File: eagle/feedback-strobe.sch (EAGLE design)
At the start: 21 parts, among them J2 MOTOR, U1 STN3NF06L, U2 +12v

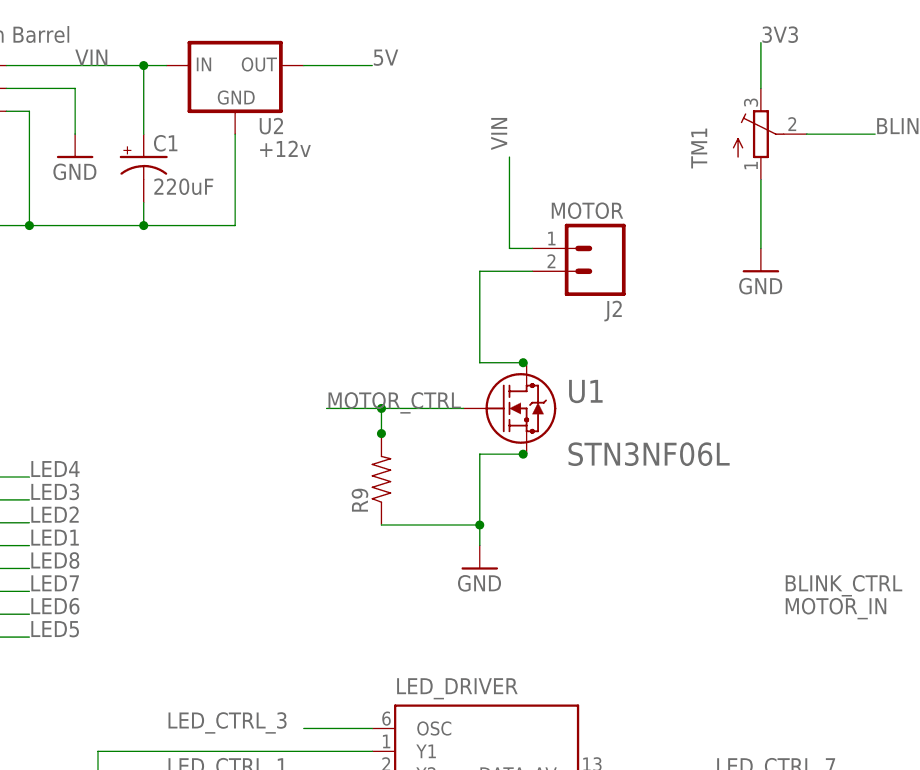
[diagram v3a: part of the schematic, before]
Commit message: added new voltage regulator, reduced number of vias, added more spacing between traces.
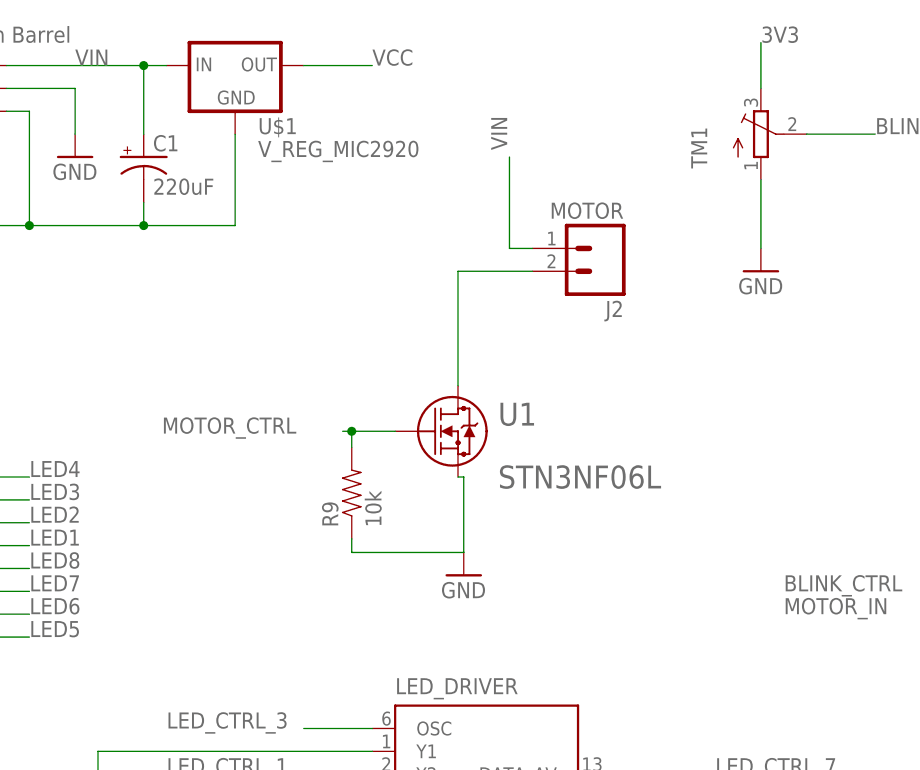
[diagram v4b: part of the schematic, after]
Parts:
- removed U2: +12v, SparkFun-PowerIC:V_REG_78XX7812
- added U$1: V_REG_MIC2920, SparkFun-PowerIC:V_REG_MIC2920
- R9: value (none) -> 10k
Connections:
- removed net N$8: J2.2
- new net N$7: J2.2, U1.2
- new net VCC: U$1.OUT
- net 5V: no longer U2.OUT
- net GND: now also U$1.GND, U1.3; no longer U2.GND
- net VIN: now also U$1.IN; no longer U2.IN
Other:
- moved on the sheet: R9, U1
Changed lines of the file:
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@@
 <setting verticaltext="up"/>
 </settings>
-<grid distance="0.01" unitdist="inch" unit="inch" style="lines" multiple="1" display="no" altdistance="0.01" altunitdist="inch" altunit="inch"/>
+<grid distance="0.1" unitdist="inch" unit="inch" style="lines" multiple="1" display="no" altdistance="0.01" altunitdist="inch" altunit="inch"/>
 <layers>
 <layer number="1" name="Top" color="4" fill="1" visible="no" active="no"/>
@@
 <part name="J2" library="SparkFun-Connectors" deviceset="M02" device="PTH" value="MOTOR"/>
 <part name="DC_IN" library="SparkFun-Connectors" deviceset="POWER_JACK" device="SMD" value="5.5x2.1mm Barrel"/>
-<part name="U2" library="SparkFun-PowerIC" deviceset="V_REG_78XX" device="7812" value="+12v"/>
 <part name="TEENSY" library="SparkFun-Connectors" deviceset="M13" device=""/>
 <part name="IR" library="SparkFun-Connectors" deviceset="M02" device="PTH"/>
@@
 <part name="GND6" library="SparkFun-Aesthetics" deviceset="GND" device=""/>
 <part name="GND7" library="SparkFun-Aesthetics" deviceset="GND" device=""/>
-<part name="GND1" library="SparkFun-Aesthetics" deviceset="GND" device=""/>
-<part name="R9" library="SparkFun-Passives" deviceset="RESISTOR" device="0603-RES"/>
 <part name="J3" library="SparkFun-Connectors" deviceset="M01" device="PTH"/>
 <part name="TM1" library="adafruit" deviceset="TRIMPOT" device="3386"/>
@@
 <part name="J1" library="SparkFun-Connectors" deviceset="M03" device="PTH"/>
 <part name="GND2" library="SparkFun-Aesthetics" deviceset="GND" device=""/>
+<part name="U$1" library="SparkFun-PowerIC" deviceset="V_REG_MIC2920" device=""/>
 <part name="U1" library="n-fet" deviceset="STN3NF06L" device=""/>
+<part name="GND1" library="SparkFun-Aesthetics" deviceset="GND" device=""/>
+<part name="R9" library="SparkFun-Passives" deviceset="RESISTOR" device="0603-RES" value="10k"/>
 </parts>
 <sheets>
@@
 <instance part="J2" gate="G$1" x="55.88" y="106.68" rot="R180"/>
 <instance part="DC_IN" gate="G$1" x="-12.7" y="119.38"/>
-<instance part="U2" gate="G$1" x="15.24" y="127"/>
 <instance part="TEENSY" gate="G$1" x="127" y="81.28" rot="R180"/>
 <instance part="IR" gate="G$1" x="122.936" y="129.54" rot="R180"/>
@@
 <instance part="GND6" gate="1" x="0" y="45.72"/>
 <instance part="GND7" gate="1" x="99.06" y="30.48"/>
-<instance part="GND1" gate="1" x="42.418" y="71.12"/>
-<instance part="R9" gate="G$1" x="31.496" y="81.026" rot="R90"/>
 <instance part="J3" gate="G$1" x="124.46" y="53.34" rot="R180"/>
 <instance part="TM1" gate="G$1" x="73.66" y="119.38"/>
@@
 <instance part="J1" gate="J$1" x="124.46" y="111.76" rot="R180"/>
 <instance part="GND2" gate="1" x="111.76" y="101.6"/>
-<instance part="U1" gate="A" x="40.64" y="88.9"/>
+<instance part="U$1" gate="G$1" x="15.24" y="127"/>
+<instance part="U1" gate="A" x="33.02" y="86.36"/>
+<instance part="GND1" gate="1" x="40.64" y="70.358"/>
+<instance part="R9" gate="G$1" x="28.194" y="79.502" rot="R90"/>
 </instances>
 <busses>
@@
 <net name="GND" class="0">
 <segment>
-<pinref part="U2" gate="G$1" pin="GND"/>
 <wire x1="15.24" y1="119.38" x2="15.24" y2="109.22" width="0.1524" layer="91"/>
 <wire x1="15.24" y1="109.22" x2="5.08" y2="109.22" width="0.1524" layer="91"/>
@@
 <wire x1="-7.62" y1="109.22" x2="-35.56" y2="109.22" width="0.1524" layer="91"/>
 <wire x1="-35.56" y1="109.22" x2="-35.56" y2="106.68" width="0.1524" layer="91"/>
+<pinref part="U$1" gate="G$1" pin="GND"/>
 </segment>
 <segment>
@@
 </segment>
 <segment>
-<pinref part="GND1" gate="1" pin="GND"/>
-<pinref part="R9" gate="G$1" pin="1"/>
-<wire x1="42.418" y1="75.946" x2="42.418" y2="73.66" width="0.1524" layer="91"/>
-<wire x1="31.496" y1="75.946" x2="42.418" y2="75.946" width="0.1524" layer="91"/>
-<junction x="42.418" y="75.946"/>
-<wire x1="42.418" y1="75.946" x2="42.672" y2="75.946" width="0.1524" layer="91"/>
-<wire x1="42.418" y1="83.82" x2="42.418" y2="75.946" width="0.1524" layer="91"/>
-<wire x1="42.418" y1="83.82" x2="47.244" y2="83.82" width="0.1524" layer="91"/>
-<junction x="47.244" y="83.82"/>
-</segment>
-<segment>
 <pinref part="TM1" gate="G$1" pin="A"/>
 <wire x1="73.66" y1="114.3" x2="73.66" y2="106.68" width="0.1524" layer="91"/>
@@
 <pinref part="GND2" gate="1" pin="GND"/>
 </segment>
+<segment>
+<pinref part="U1" gate="A" pin="3"/>
+<pinref part="GND1" gate="1" pin="GND"/>
+<wire x1="40.005" y1="81.28" x2="40.64" y2="81.28" width="0.1524" layer="91"/>
+<wire x1="40.64" y1="81.28" x2="40.64" y2="72.898" width="0.1524" layer="91"/>
+<pinref part="R9" gate="G$1" pin="1"/>
+<wire x1="40.64" y1="72.898" x2="28.194" y2="72.898" width="0.1524" layer="91"/>
+<wire x1="28.194" y1="72.898" x2="28.194" y2="74.422" width="0.1524" layer="91"/>
+</segment>
 </net>
 <net name="VIN" class="0">
 <segment>
 <pinref part="DC_IN" gate="G$1" pin="PWR"/>
-<pinref part="U2" gate="G$1" pin="IN"/>
 <wire x1="-10.16" y1="127" x2="5.08" y2="127" width="0.1524" layer="91"/>
 <wire x1="5.08" y1="127" x2="7.62" y2="127" width="0.1524" layer="91"/>
@@
 <junction x="5.08" y="127"/>
 <label x="-2.54" y="127" size="1.778" layer="95"/>
+<pinref part="U$1" gate="G$1" pin="IN"/>
 </segment>
 <segment>
@@
 <net name="5V" class="0">
 <segment>
-<pinref part="U2" gate="G$1" pin="OUT"/>
-<wire x1="22.86" y1="127" x2="30.48" y2="127" width="0.1524" layer="91"/>
-<label x="30.48" y="127" size="1.778" layer="95"/>
-</segment>
-<segment>
 <pinref part="TEENSY" gate="G$1" pin="1"/>
 <wire x1="116.84" y1="96.52" x2="109.22" y2="96.52" width="0.1524" layer="91"/>
@@
 <segment>
 <pinref part="U1" gate="A" pin="1"/>
-<wire x1="40.64" y1="88.9" x2="31.496" y2="88.9" width="0.1524" layer="91"/>
-<label x="25.4" y="88.9" size="1.778" layer="95"/>
+<wire x1="33.02" y1="86.36" x2="28.194" y2="86.36" width="0.1524" layer="91"/>
 <pinref part="R9" gate="G$1" pin="2"/>
-<wire x1="31.496" y1="88.9" x2="25.4" y2="88.9" width="0.1524" layer="91"/>
-<wire x1="31.496" y1="86.106" x2="31.496" y2="88.9" width="0.1524" layer="91"/>
-<junction x="31.496" y="86.106"/>
-<junction x="31.496" y="88.9"/>
+<wire x1="28.194" y1="84.582" x2="28.194" y2="86.36" width="0.1524" layer="91"/>
+<wire x1="28.194" y1="86.36" x2="27.178" y2="86.36" width="0.1524" layer="91"/>
+<label x="7.112" y="86.106" size="1.778" layer="95"/>
+<junction x="28.194" y="86.36"/>
 </segment>
 </net>
@@
 </segment>
 </net>
-<net name="N$8" class="0">
-<segment>
-<pinref part="J2" gate="G$1" pin="2"/>
-<wire x1="48.26" y1="104.14" x2="42.418" y2="104.14" width="0.1524" layer="91"/>
-<wire x1="42.418" y1="93.98" x2="42.418" y2="104.14" width="0.1524" layer="91"/>
-<wire x1="42.418" y1="93.98" x2="47.244" y2="93.98" width="0.1524" layer="91"/>
-<junction x="47.244" y="93.98"/>
-</segment>
-</net>
 <net name="BLINK_CTRL" class="0">
 <segment>
@@
 </segment>
 </net>
+<net name="VCC" class="0">
+<segment>
+<wire x1="22.86" y1="127" x2="30.48" y2="127" width="0.1524" layer="91"/>
+<label x="30.48" y="127" size="1.778" layer="95"/>
+<pinref part="U$1" gate="G$1" pin="OUT"/>
+</segment>
+</net>
+<net name="N$7" class="0">
+<segment>
+<pinref part="J2" gate="G$1" pin="2"/>
+<pinref part="U1" gate="A" pin="2"/>
+<wire x1="48.26" y1="104.14" x2="40.005" y2="104.14" width="0.1524" layer="91"/>
+<wire x1="40.005" y1="104.14" x2="40.005" y2="91.44" width="0.1524" layer="91"/>
+</segment>
+</net>
